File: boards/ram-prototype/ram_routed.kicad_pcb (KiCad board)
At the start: 4 copper layers, 217 x 107 mm, 512 parts, among them J1 PinHeader_1x16_P2.54mm_Vertic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, U1 DSBGA-5_NumericPads, U10 DSBGA-6_NumericPads, U100 DSBGA-5_NumericPads, U101 DSBGA-5_NumericPads, U102 DSBGA-5_NumericPads, U103 DSBGA-5_NumericPads, U104 DSBGA-5_NumericPads, U105 DSBGA-5_NumericPads, U106 DSBGA-5_NumericPads, U107 DSBGA-5_NumericPads, U108 DSBGA-5_NumericPads, U109 DSBGA-5_NumericPads, U11 DSBGA-6_NumericPads, U110 DSBGA-5_NumericPads, U111 DSBGA-5_NumericPads, U112 DSBGA-5_NumericPads, U113 DSBGA-5_NumericPads, U114 DSBGA-5_NumericPads, U115 DSBGA-5_NumericPads, U116 DSBGA-5_NumericPads, U117 DSBGA-5_NumericPads, U118 DSBGA-5_NumericPads, U119 DSBGA-5_NumericPads, U12 DSBGA-5_NumericPads, U120 DSBGA-5_NumericPads, U121 DSBGA-5_NumericPads, U122 DSBGA-5_NumericPads, U123 DSBGA-5_NumericPads, U124 DSBGA-5_NumericPads, U125 DSBGA-5_NumericPads, U126 DSBGA-5_NumericPads, U127 DSBGA-5_NumericPads, U128 DSBGA-5_NumericPads, U129 DSBGA-5_NumericPads, U13 DSBGA-5_NumericPads, U130 DSBGA-5_NumericPads, U131 DSBGA-5_NumericPads, U132 DSBGA-5_NumericPads, U133 DSBGA-5_NumericPads, U134 DSBGA-5_NumericPads, U135 DSBGA-5_NumericPads, U136 DSBGA-5_NumericPads, U137 DSBGA-5_NumericPads, U138 DSBGA-5_NumericPads, U139 DSBGA-5_NumericPads, U14 DSBGA-5_NumericPads, U140 DSBGA-5_NumericPads, U141 DSBGA-5_NumericPads, U142 DSBGA-5_NumericPads, U143 DSBGA-5_NumericPads, U144 DSBGA-5_NumericPads, U145 DSBGA-5_NumericPads, U146 DSBGA-5_NumericPads, U147 DSBGA-5_NumericPads, U148 DSBGA-5_NumericPads, U149 DSBGA-5_NumericPads, U15 DSBGA-5_NumericPads, U150 DSBGA-5_NumericPads, U151 DSBGA-5_NumericPads, U152 DSBGA-5_NumericPads, U153 DSBGA-5_NumericPads, U154 DSBGA-5_NumericPads, U155 DSBGA-5_NumericPads, U156 DSBGA-5_NumericPads, U157 DSBGA-5_NumericPads, U158 DSBGA-5_NumericPads, U159 DSBGA-5_NumericPads, U16 DSBGA-5_NumericPads, U160 DSBGA-5_NumericPads, U161 DSBGA-5_NumericPads, U17 DSBGA-5_NumericPads, U18 DSBGA-5_NumericPads, U19 DSBGA-5_NumericPads, U2 DSBGA-5_NumericPads, U20 DSBGA-5_NumericPads, U21 DSBGA-5_NumericPads, U22 DSBGA-5_NumericPads, U23 DSBGA-5_NumericPads, U24 DSBGA-5_NumericPads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

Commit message: fix some of the routing
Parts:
- J1: value PinHeader_1x16_P2.54mm_Vertical -> PinHeader_1x16_P2\.54mm_Vertical
- U1, U100, U101, U102, U103, U104, U105, U106, U107, U108, U109, U110, U111, U112, U113, U114, U115, U116, U117, U118, U119, U12, U120, U121, U122, U123, U124, U125, U126, U127, U128, U129, U13, U130, U131, U132, U133, U134, U135, U136, U137, U138, U139, U14, U140, U141, U142, U143, U144, U145, U146, U147, U148, U149, U15, U150, U151, U152, U153, U154, U155, U156, U157, U158, U159, U16, U160, U161, U17, U18, U19, U2, U20, U21, U22, U23, U24, U25, U26, U27, U28, U29, U3, U30, U31, U32, U33, U34, U35, U36, U37, U38, U39, U40, U41, U42, U43, U44, U45, U46, U47, U48, U49, U50, U51, U52, U53, U54, U55, U56, U57, U58, U59, U60, U61, U62, U63, U64, U65, U66, U67, U68, U69, U70, U71, U72, U73, U74, U75, U76, U77, U78, U79, U80, U81, U82, U83, U84, U85, U86, U87, U88, U89, U90, U91, U92, U93, U94, U95, U96, U97, U98, U99: value DSBGA-5_NumericPads -> DSBGA\-5_NumericPads
- U10, U11, U4, U5, U6, U7, U8, U9: value DSBGA-6_NumericPads -> DSBGA\-6_NumericPads
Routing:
- net /Address Decoder/SEL6: track 179.2 -> 156.0 mm, vias 4 -> 2
- net /D7: track 389.3 -> 410.5 mm
- net /Byte 4/WRITE_CLK: track 213.6 -> 228.1 mm
- net /Address Decoder/A0: track 110.1 -> 101.3 mm, vias 6 -> 4
- net /Control Logic/WRITE_ACTIVE: track 157.8 -> 149.4 mm
- net /D4: track 363.2 -> 355.9 mm, vias 19 -> 18
- net /D1: track 335.2 -> 340.8 mm, vias 19 -> 18
- net /Control Logic/nWE: track 56.8 -> 62.3 mm
- net /Address Decoder/A1: track 104.8 -> 99.4 mm, vias 5 -> 6
- net Net-(R15-Pad1): track 47.1 -> 42.0 mm, vias 2 -> 5
- net /D0: track 336.0 -> 340.4 mm
- net /Byte 6/WRITE_CLK: track 188.7 -> 192.8 mm
- net /Byte 3/WRITE_CLK: track 97.1 -> 93.1 mm
- net /Address Decoder/SEL7: track 154.0 -> 157.9 mm
- net /BUF_OE_4: track 171.7 -> 175.5 mm
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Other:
- outline, holes or cut-outs redrawn

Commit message: rearange some components
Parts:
- moved D160 52.5 mm to (95.5, 19.0)
- moved D161 52.5 mm to (95.5, 40.0)
- moved D162 52.5 mm to (95.5, 61.0)
- moved D163 52.5 mm to (95.5, 82.0)
- moved D164 52.5 mm to (170.0, 19.0)
- moved D165 52.5 mm to (170.0, 40.0)
- moved D166 52.5 mm to (170.0, 61.0)
- moved D167 52.5 mm to (170.0, 82.0)
- moved D168 52.5 mm to (95.5, 23.5)
- moved D169 52.5 mm to (95.5, 44.5)
- moved D170 52.5 mm to (95.5, 65.5)
- moved D171 52.5 mm to (95.5, 86.5)
- moved D172 52.5 mm to (170.0, 23.5)
- moved D173 52.5 mm to (170.0, 44.5)
- moved D174 52.5 mm to (170.0, 65.5)
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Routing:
- net /D7: track 410.5 -> 335.8 mm, vias 16 -> 17
- net /D0: track 340.4 -> 393.8 mm
- net /D6: track 369.6 -> 333.8 mm
- net /Address Decoder/A0: track 101.3 -> 67.3 mm, vias 4 -> 3
- net /D1: track 340.8 -> 373.0 mm
- net /D5: track 373.8 -> 342.4 mm, vias 18 -> 19
- net /Address Decoder/A1: track 99.4 -> 69.1 mm, vias 6 -> 2
- net /Address Decoder/A2: track 112.2 -> 84.9 mm, vias 3 -> 5
- net /Address Decoder/SEL5: track 176.2 -> 154.6 mm
- net /D2: track 342.5 -> 363.0 mm, vias 19 -> 18
- net /Control Logic/nCE: track 47.9 -> 29.6 mm, vias 2 -> 0
- net /Control Logic/nOE: track 54.5 -> 36.9 mm, vias 2 -> 0
- net /Control Logic/nWE: track 62.3 -> 77.3 mm, vias 2 -> 0
- net /Byte 4/WRITE_CLK: track 228.1 -> 217.1 mm
- net Net-(R28-Pad1): track 31.0 -> 21.9 mm
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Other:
- board text added: "0x0"
- board text added: "0x1"
- board text added: "0x2"
- board text added: "0x3"
- board text added: "0x4"
- board text added: "0x5"
- board text added: "0x6"
- board text added: "0x7"

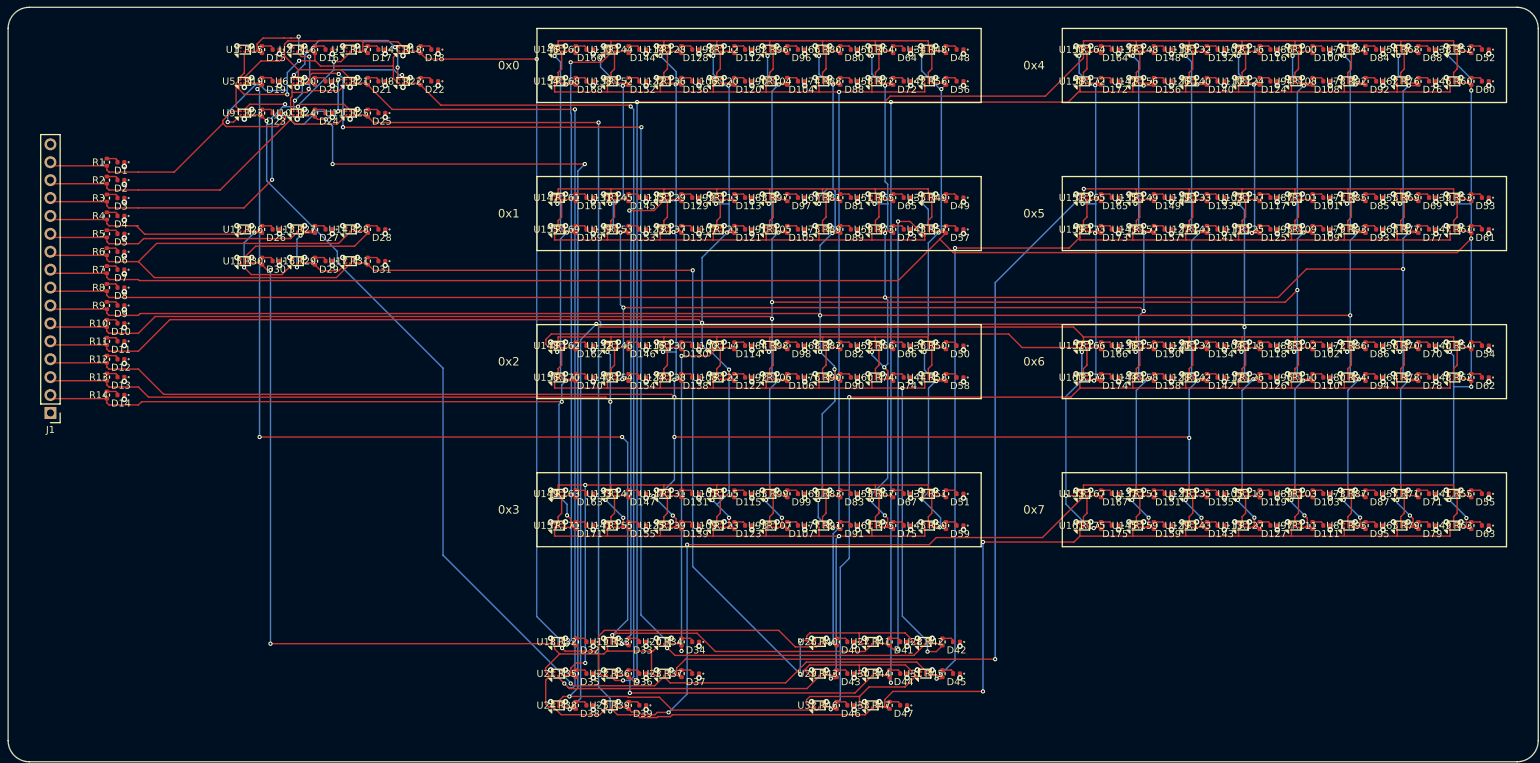
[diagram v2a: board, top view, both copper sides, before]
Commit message: Clean up silkscreen
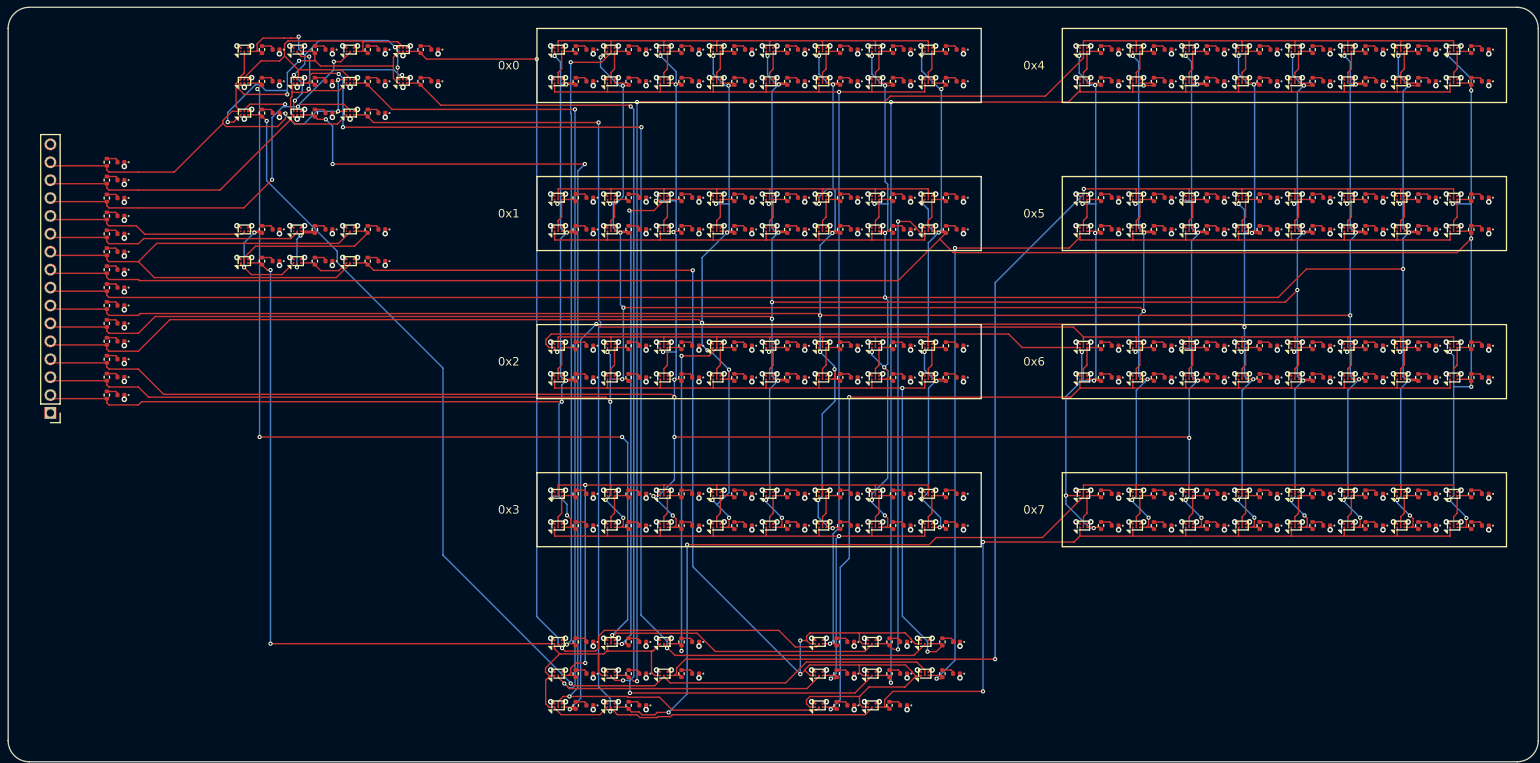
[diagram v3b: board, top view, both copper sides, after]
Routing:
- net GND: track 255.0 -> 202.5 mm
